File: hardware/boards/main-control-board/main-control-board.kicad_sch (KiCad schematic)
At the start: 10 parts, among them J1 Conn_MAX98357, J2 Conn_OLED, J3 Conn_PCA9685_1, J4 Conn_PCA9685_2, J5 Conn_ESP32_R, J6 Conn_ESP32_L, J7 Conn_USB

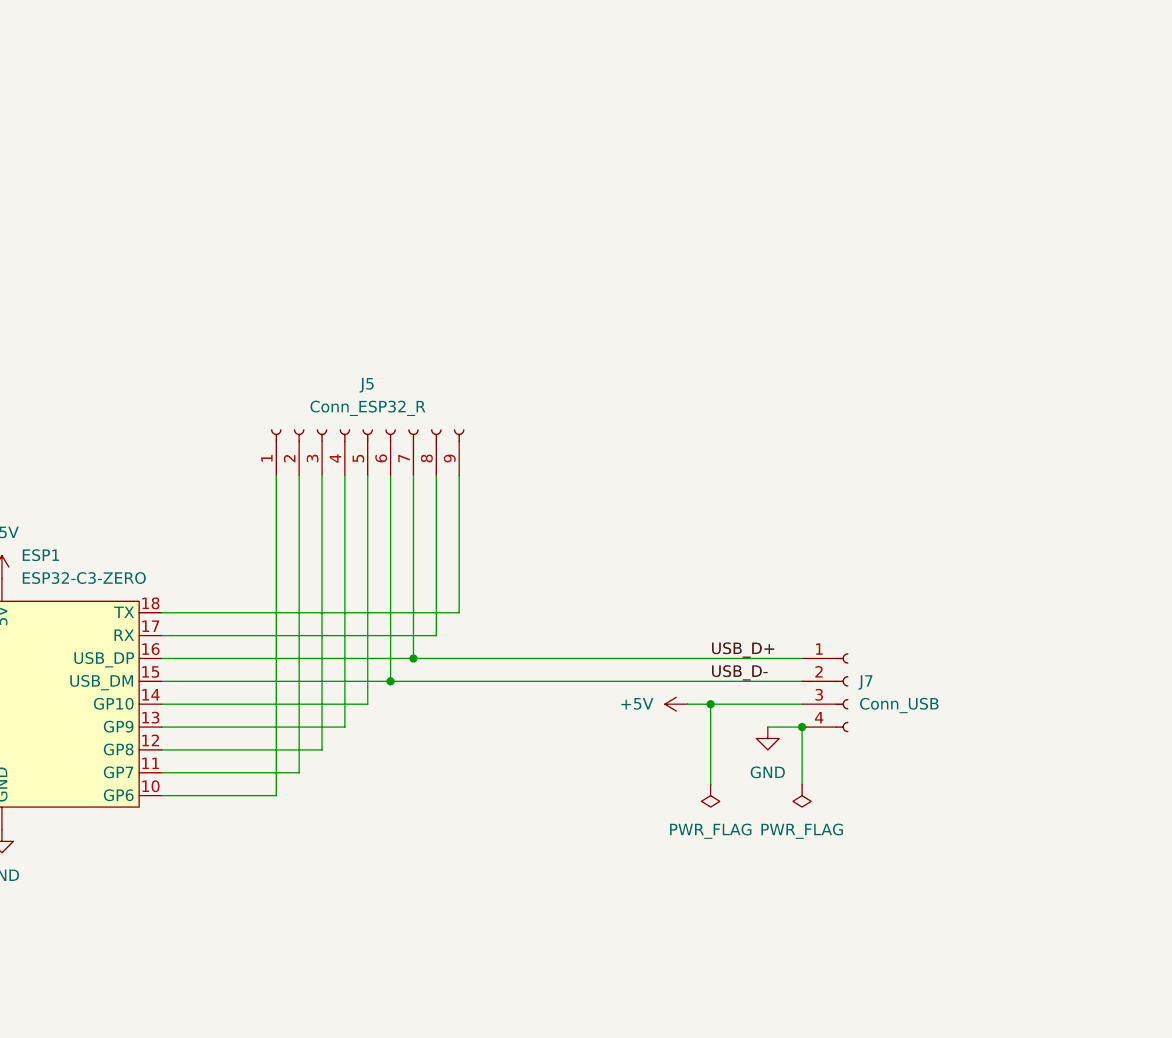
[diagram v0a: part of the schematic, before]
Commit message: reshape the board to mount SDM USB
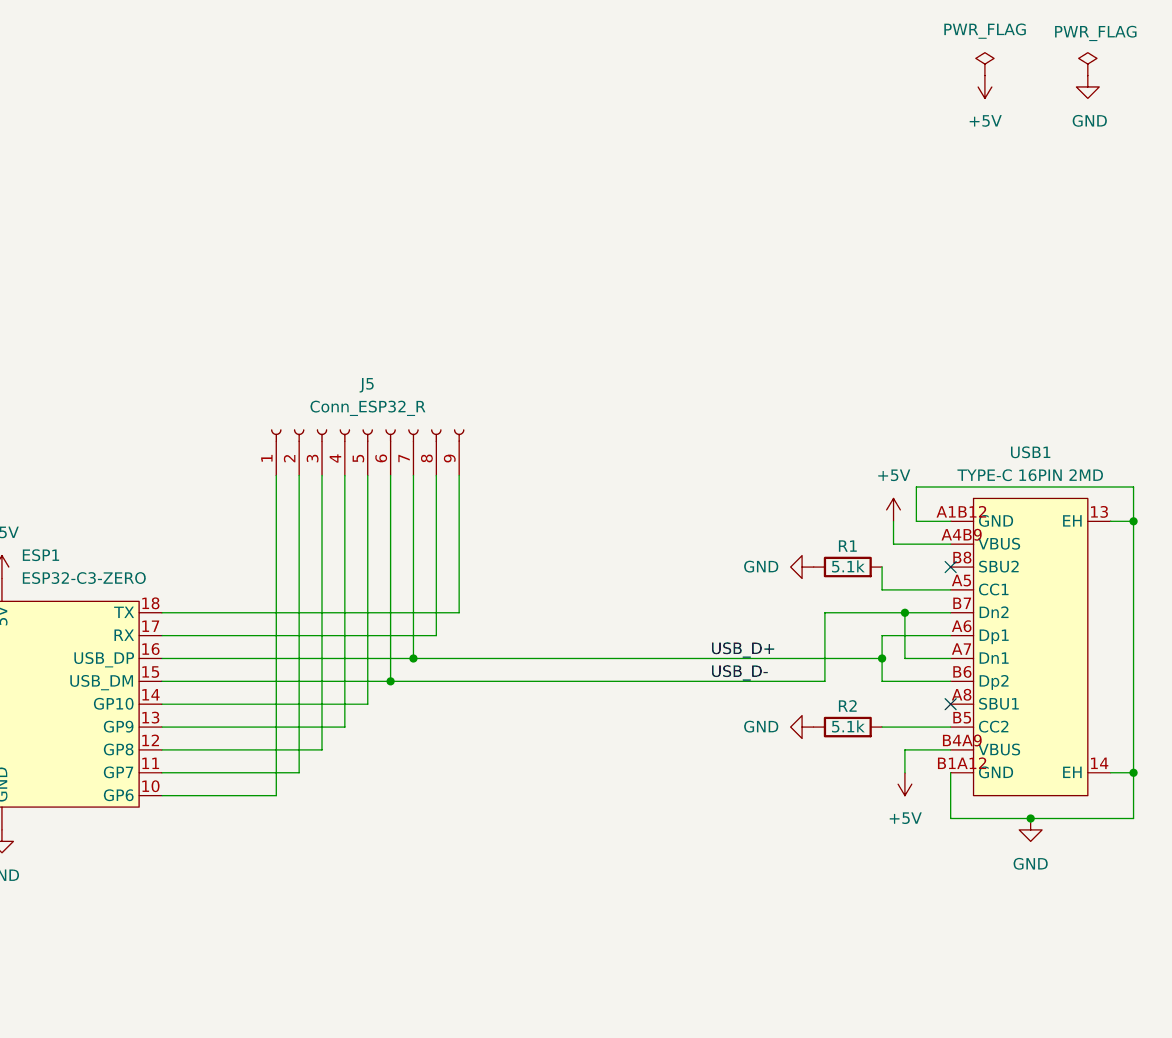
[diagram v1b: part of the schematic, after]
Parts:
- removed J7: Conn_USB, Connector_PinSocket_2.54mm:PinSocket_1x04_P2.54mm_Vertical, symbol Connector:Conn_01x04_Socket
- added R1, R2: 5.1k, Resistor_SMD:R_0603_1608Metric, symbol Device:R
- added USB1: TYPE-C 16PIN 2MD, easyeda:USB-C-SMD_TYPE-C-16PIN-2MD-073, symbol easyeda:TYPE-C16PIN2MD
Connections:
- net +5V: now also USB1.A4B9 (VBUS), USB1.B4A9 (VBUS)
- net GND: now also R1.1, R2.1, USB1.13 (EH), USB1.14 (EH), USB1.A1B12 (GND), USB1.B1A12 (GND)
- net USB_D+: now also USB1.A6 (Dp1), USB1.B6 (Dp2)
- net USB_D-: now also USB1.A7 (Dn1), USB1.B7 (Dn2)
- new net: R2.2, USB1.B5 (CC2)
- new net: R1.2, USB1.A5 (CC1)
- no-connect marks 0 -> 2

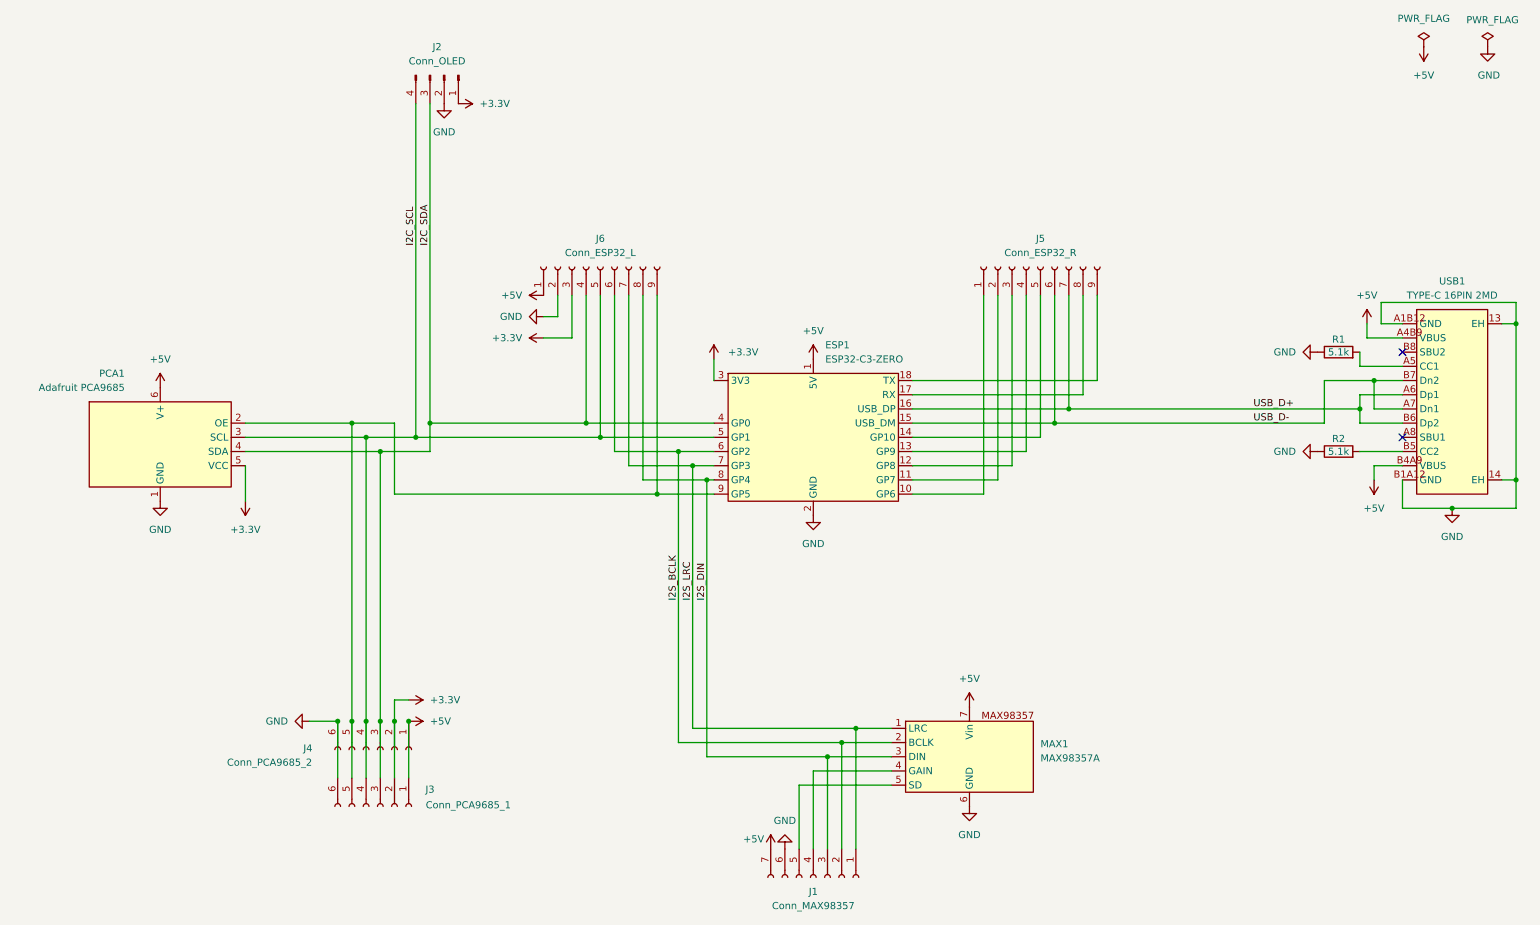
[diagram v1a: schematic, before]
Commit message: use hierarchical sheets in schmatic
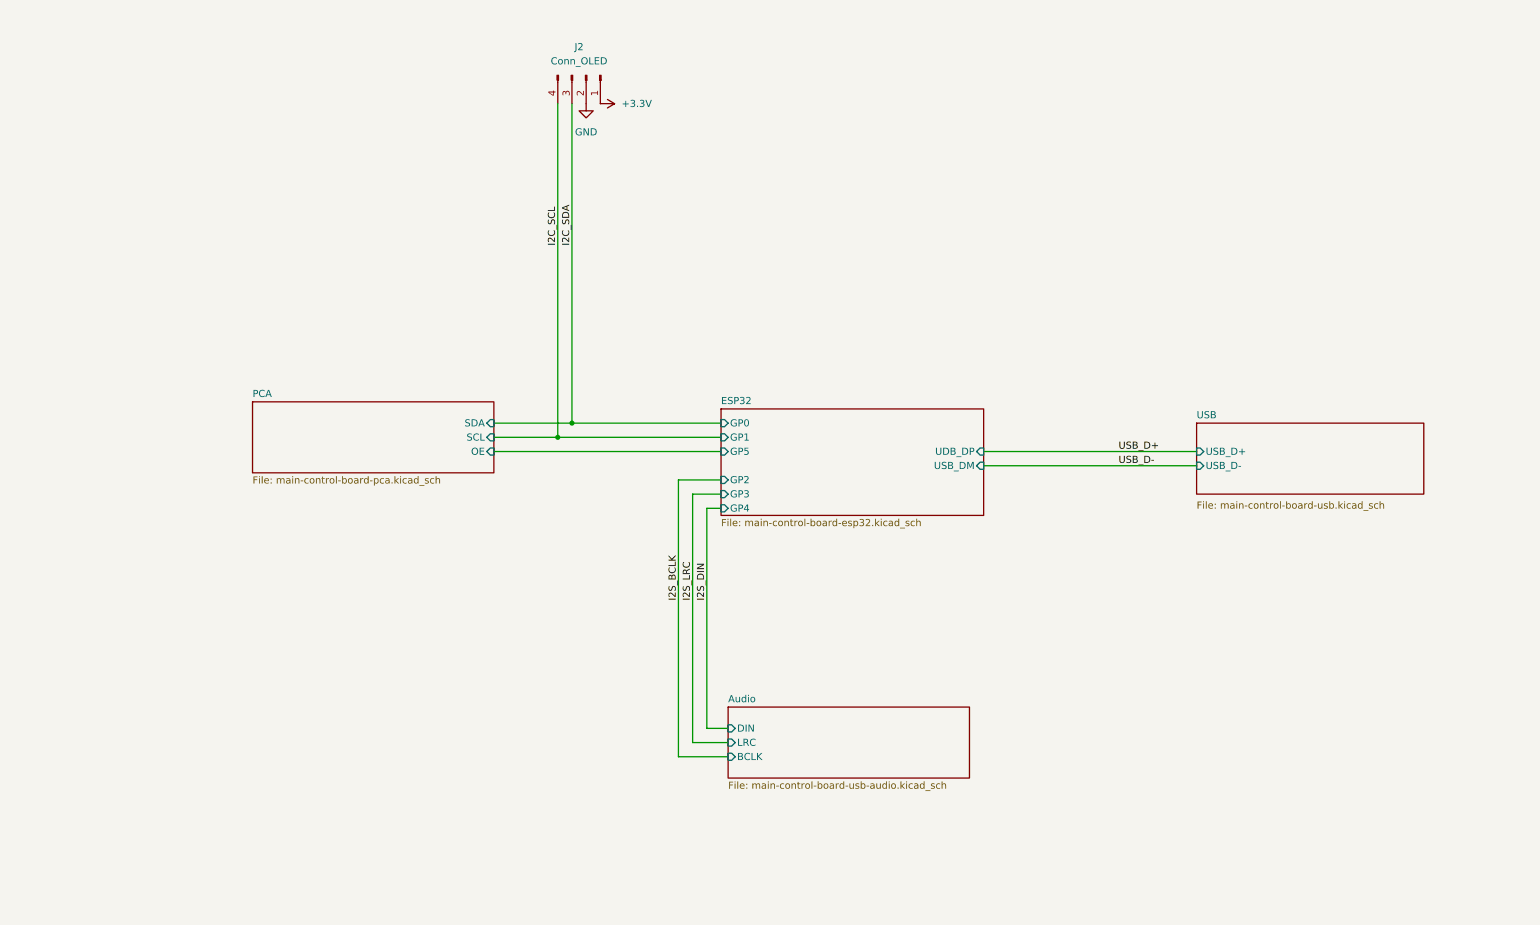
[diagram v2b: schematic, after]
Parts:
- removed ESP1: ESP32-C3-ZERO, TinyEngineerModules:ESP32_C3_Zero_Dev_Board, symbol TinyEngineerModules:ESP32_C3_Zero_Dev_Board
- removed J1: Conn_MAX98357, Connector_PinSocket_2.54mm:PinSocket_1x07_P2.54mm_Vertical, symbol Connector:Conn_01x07_Socket
- removed J3: Conn_PCA9685_1, Connector_PinSocket_2.54mm:PinSocket_1x06_P2.54mm_Vertical, symbol Connector:Conn_01x06_Socket
- removed J4: Conn_PCA9685_2, Connector_PinSocket_2.54mm:PinSocket_1x06_P2.54mm_Vertical, symbol Connector:Conn_01x06_Socket
- removed J5: Conn_ESP32_R, Connector_PinSocket_2.54mm:PinSocket_1x09_P2.54mm_Vertical, symbol Connector:Conn_01x09_Socket
- removed J6: Conn_ESP32_L, Connector_PinSocket_2.54mm:PinSocket_1x09_P2.54mm_Vertical, symbol Connector:Conn_01x09_Socket
- removed MAX1: MAX98357A, symbol TinyEngineerModules:MAX98357_Module
- removed PCA1: Adafruit PCA9685, symbol TinyEngineerModules:Adafruit_PCA9685_Module
- removed R1, R2: 5.1k, Resistor_SMD:R_0603_1608Metric, symbol Device:R
- removed USB1: TYPE-C 16PIN 2MD, easyeda:USB-C-SMD_TYPE-C-16PIN-2MD-073, symbol easyeda:TYPE-C16PIN2MD
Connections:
- no-connect marks 2 -> 0
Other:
- added sheet Audio (main-control-board-usb-audio.kicad_sch)
- added sheet ESP32 (main-control-board-esp32.kicad_sch)
- added sheet PCA (main-control-board-pca.kicad_sch)
- added sheet USB (main-control-board-usb.kicad_sch)
- moved on the sheet: J2

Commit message: integrate PCA into the board
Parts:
- J2: FT Rotation Offset 90 -> (none)
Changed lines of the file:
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@@
-			)
-		)
-		(property "FT Rotation Offset" "90"
-			(at 115.57 25.4 90)
-			(hide yes)
-			(show_name no)
-			(do_not_autoplace no)
-			(effects
-				(font
-					(size 1.27 1.27)
-				)
 			)
 		)

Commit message: set FT Rotation Offset to fix JLCPCB orientation
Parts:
- J2: FT Rotation Offset (none) -> 90
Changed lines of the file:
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@@
+			)
+		)
+		(property "FT Rotation Offset" "90"
+			(at 115.57 25.4 90)
+			(hide yes)
+			(show_name no)
+			(do_not_autoplace no)
+			(effects
+				(font
+					(size 1.27 1.27)
+				)
 			)
 		)

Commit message: add I2C extension port
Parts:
- added H1, H2: MountingHole, MountingHole:MountingHole_2.2mm_M2, symbol Mechanical:MountingHole
- added J3: Conn_extension, Connector_JST:JST_SH_SM04B-SRSS-TB_1x04-1MP_P1.00mm_Horizontal, symbol Connector_Generic:Conn_01x04
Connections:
- net +3.3V: now also J3.2 (Pin_2)
- net GND: now also J3.1 (Pin_1)
- net I2C_SCL: now also J3.4 (Pin_4)
- net I2C_SDA: now also J3.3 (Pin_3)

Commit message: use basic components over extended
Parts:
- added D2: LED, LED_SMD:LED_0603_1608Metric, symbol Device:LED
- added R13: 1k, Resistor_SMD:R_0603_1608Metric, symbol Device:R
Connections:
- net +3.3V: now also R13.1
- net GND: now also D2.1 (K)
- new net: D2.2 (A), R13.2

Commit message: add polyfuse protection
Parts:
- added TP3: TestPointGND, TestPoint:TestPoint_THTPad_1.5x1.5mm_Drill0.7mm, symbol Connector:TestPoint
- added TP4: TestPoint5V, TestPoint:TestPoint_THTPad_1.5x1.5mm_Drill0.7mm, symbol Connector:TestPoint
- added TP5: TestPoint3.3V, TestPoint:TestPoint_THTPad_1.5x1.5mm_Drill0.7mm, symbol Connector:TestPoint
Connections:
- net +3.3V: now also TP5.1
- net GND: now also TP3.1
- new net +5V: TP4.1

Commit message: turn test points into extension points
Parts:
- removed TP3: TestPointGND, TestPoint:TestPoint_THTPad_1.5x1.5mm_Drill0.7mm, symbol Connector:TestPoint
- removed TP4: TestPoint5V, TestPoint:TestPoint_THTPad_1.5x1.5mm_Drill0.7mm, symbol Connector:TestPoint
- removed TP5: TestPoint3.3V, TestPoint:TestPoint_THTPad_1.5x1.5mm_Drill0.7mm, symbol Connector:TestPoint
- added J4: Conn_extension_2, Connector_PinHeader_2.54mm:PinHeader_1x04_P2.54mm_Vertical, symbol Connector_Generic:Conn_01x04
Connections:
- net +3.3V: now also J4.2 (Pin_2)
- net +5V: now also J4.1 (Pin_1)
- net GND: now also J4.3 (Pin_3)
- new net ESP32/GP6: J4.4 (Pin_4)
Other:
- sheet ESP32 ports: added GP6; removed none
